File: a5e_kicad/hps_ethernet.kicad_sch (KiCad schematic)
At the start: 53 parts, among them J9 RJ45_RB1-125B8G1A, U10 RTL8211FDI-CG, Y3 25MHz

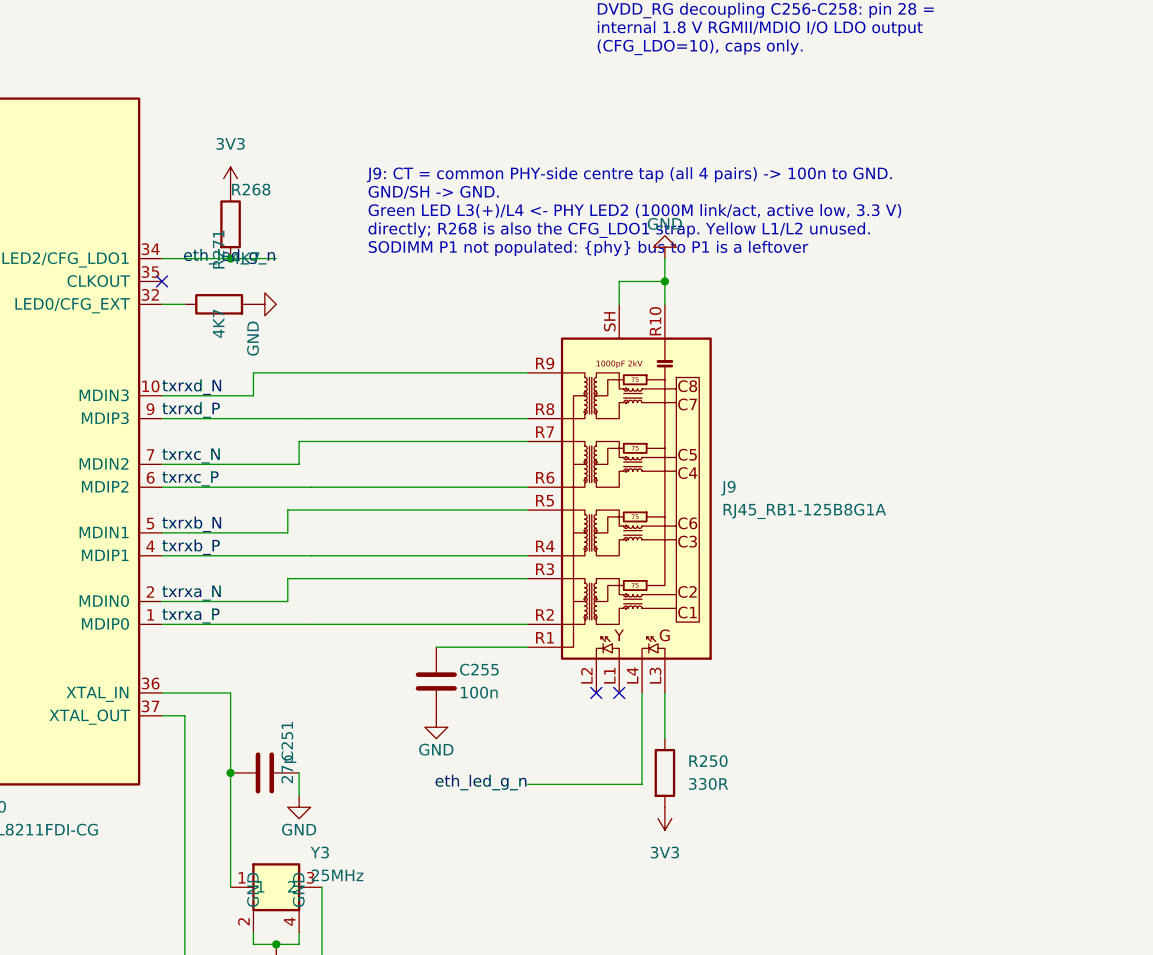
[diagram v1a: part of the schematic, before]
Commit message: J9 MagJack to HanRun HR911130A with the Zynq board's PHY layout
- J9: UDE RB1-125B8G1A (oversold at JLC) replaced by HanRun HR911130A
  (LCSC C54408), symbol and footprint from the Zynq board; nets eth_ct and
  eth_led_a named
- PHY area copied from the Zynq board: U10 rotated to 180 deg, passives in
  the Zynq positions, J9 at the Zynq edge offset, MDI pairs copied; block
  2 mm higher to clear U11. R251-R256 stay next to U10, C30-C32 under U10
- Old PHY-local routing, RGMII/MDIO pieces in the PHY area and conflicting
  GND/1V2 copper removed; RGMII/MDIO/PHY routing to redo
- Includes the pending board edits (zone refill etc.)

ERC 0, DRC parity 0. DRC (refilled) 150 vs 201 before; 44 new unconnected.
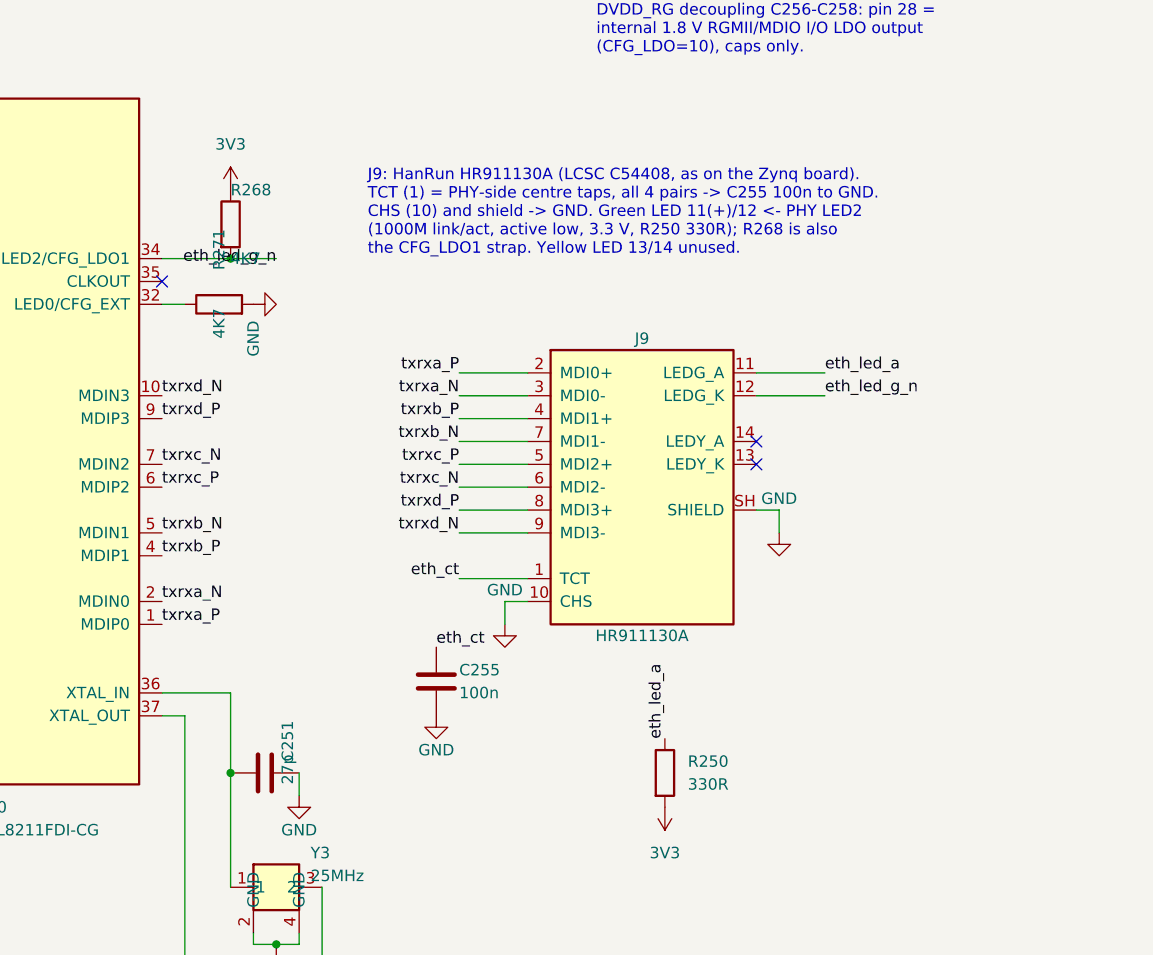
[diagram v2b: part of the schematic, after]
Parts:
- J9: value RJ45_RB1-125B8G1A -> HR911130A; footprint Connector_RJ:RJ45_UDE_RB1-125B8G1A -> agilex_lib:RJ45_Hanrun_HR911130A_Horizontal; symbol Connector:RJ45_RB1-125B8G1A -> agilex_5_lib:HR911130A; LCSC C363353 -> C54408
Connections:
- net GND: now also J9.10 (CHS); no longer J9.R10 (GND)
- net eth_led_g_n: now also J9.12 (LEDG_K); no longer J9.L4
- net txrxa_N: now also J9.3 (MDI0-); no longer J9.R3 (TD1-)
- net txrxa_P: now also J9.2 (MDI0+); no longer J9.R2 (TD1+)
- net txrxb_N: now also J9.7 (MDI1-); no longer J9.R5 (TD2-)
- net txrxb_P: now also J9.4 (MDI1+); no longer J9.R4 (TD2+)
- net txrxc_N: now also J9.6 (MDI2-); no longer J9.R7 (TD3-)
- net txrxc_P: now also J9.5 (MDI2+); no longer J9.R6 (TD3+)
- net txrxd_N: now also J9.9 (MDI3-); no longer J9.R9 (TD4-)
- net txrxd_P: now also J9.8 (MDI3+); no longer J9.R8 (TD4+)
- net eth_led_a: now reaches R250.1
- net eth_led_a: now also J9.11 (LEDG_A); no longer J9.L3
- net eth_ct: now reaches C255.1
- net eth_ct: now also J9.1 (TCT); no longer J9.R1 (CT)
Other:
- note added: "J9: HanRun HR911130A (LCSC C54408, as on the Zynq board). TCT (1) = PHY-side centre taps, all 4 pairs -> C255 100n to GND. CHS (10) and shield -> GND. Green LED 11(+)/12 <- PHY LED2 (1000M link/act, active low, 3.3 V, R250 330R); R268 is also the CFG_LDO1 strap. Yellow LED 13/14 unused."
- note removed: "J9: CT = common PHY-side centre tap (all 4 pairs) -> 100n to GND. GND/SH -> GND. Green LED L3(+)/L4 <- PHY LED2 (1000M link/act, active low, 3.3 V) directly; R268 is also the CFG_LDO1 strap. Yellow L1/L2 unused. SODIMM P1 not populated: {phy} bus to P1 is a leftover"

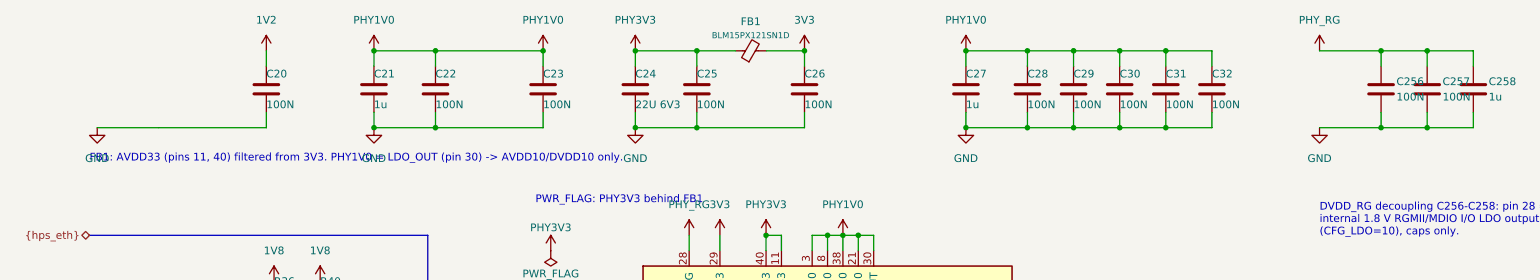
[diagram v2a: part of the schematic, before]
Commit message: Ethernet PHY: RGMII series resistors to 0201, decoupling one capacitor per pin
- R251-R262 (22R RGMII series) 0402 -> 0201, Yageo RC0201FR-0722RL (C155743); same positions, no copper attached
- removed C20 (100n on 1V2, no PHY pin uses it), C27 (second 1u on PHY1V0), C31/C32 (second caps on pins 8/38),
  C256 (second 100n on PHY_RG)
- C29 moved from PHY1V0 to PHY3V3: pin 40 (AVDD33) had no capacitor; on the board it already sits 1.4 mm from it
- per RTL8211F(D)(I)-CG data sheet Rev 1.7 9.2 and the Zynq board's U901 (ETH_PHY_REVIEW.md)
- ERC 0, schematic parity 0, DRC no new violations (unconnected 218 -> 208)
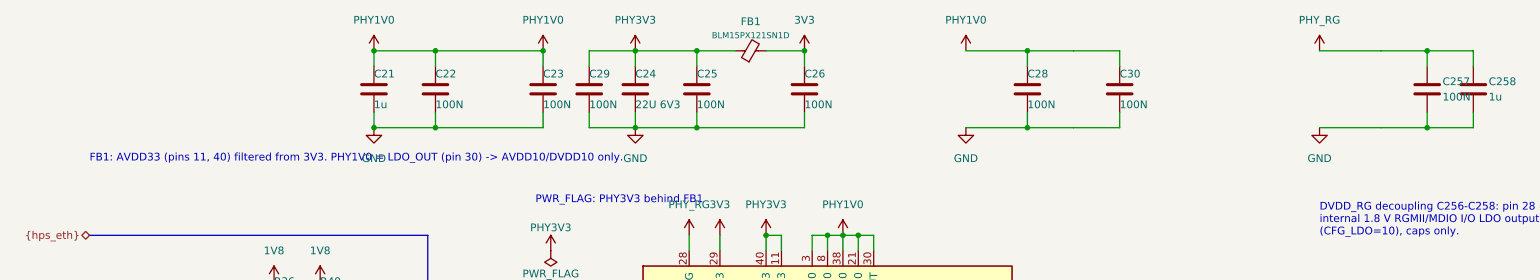
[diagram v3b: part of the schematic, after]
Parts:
- removed C20, C256, C31, C32: 100N, Capacitor_SMD:C_0402_1005Metric, symbol Device:C
- removed C27: 1u, Capacitor_SMD:C_0402_1005Metric, symbol Device:C
- R251, R252, R253, R254, R255, R256, R257, R258, R259, R260, R261, R262: footprint Resistor_SMD:R_0402_1005Metric -> Resistor_SMD:R_0201_0603Metric; LCSC C25092 -> C155743
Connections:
- net PHY1V0: no longer C29.1
- net PHY3V3: now also C29.1
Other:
- moved on the sheet: C29

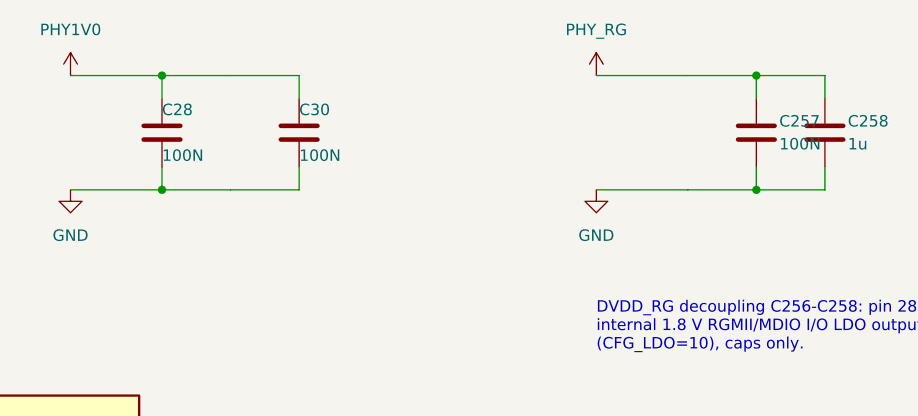
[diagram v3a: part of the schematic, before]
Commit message: Ethernet PHY passives to 0201, R27/R28 to 0402, preliminary RGMII routing
- 31 PHY passives on the hps_ethernet sheet 0402 -> 0201 (C24 22u stays
  0402): 100n C190183, 1u C272877, 27p C85899, 10k C473048,
  330R C516485, 4K7 C270346, 1K5 C270361, 2K49 C473476.
- Refclk bias R27/R28 0201 -> 0402 (C25120, 49.9R); R28 moved 0.1 mm
  to +x to clear the refclk_N meander.
- Preliminary RGMII routing: RX on F.Cu, TX on In2. Group spread
  TX 79 ps (TXD1 longest), RX 44 ps.
- Schematic sheets as saved by eeschema.
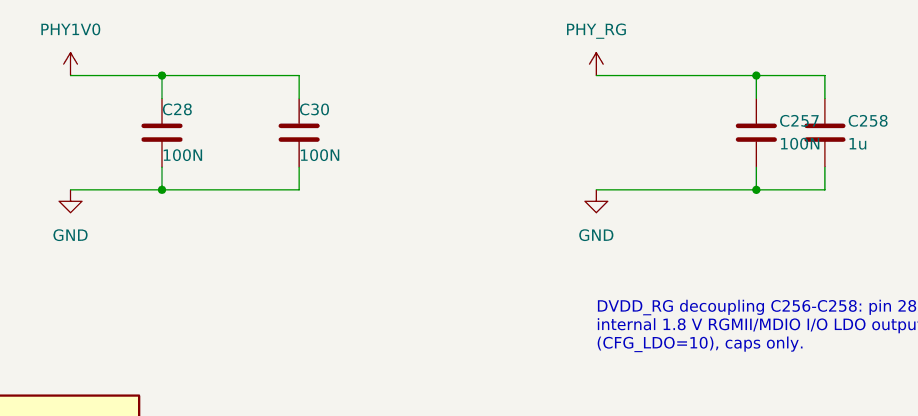
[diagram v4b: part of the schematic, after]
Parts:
- C21, C258, C259: footprint Capacitor_SMD:C_0402_1005Metric -> Capacitor_SMD:C_0201_0603Metric; LCSC C52923 -> C272877
- C22, C23, C25, C255, C257, C26, C28, C29, C30: footprint Capacitor_SMD:C_0402_1005Metric -> Capacitor_SMD:C_0201_0603Metric; LCSC C1525 -> C190183
- C251, C252: footprint Capacitor_SMD:C_0402_1005Metric -> Capacitor_SMD:C_0201_0603Metric; LCSC C1557 -> C85899
- R247: footprint Resistor_SMD:R_0402_1005Metric -> Resistor_SMD:R_0201_0603Metric; LCSC C25744 -> C473048
- R250: footprint Resistor_SMD:R_0402_1005Metric -> Resistor_SMD:R_0201_0603Metric; LCSC C25104 -> C516485
- R268, R269, R270, R271, R30, R31, R32, R33, R34, R35, R37, R39, R40: footprint Resistor_SMD:R_0402_1005Metric -> Resistor_SMD:R_0201_0603Metric; LCSC C25900 -> C270346
- R36: footprint Resistor_SMD:R_0402_1005Metric -> Resistor_SMD:R_0201_0603Metric; LCSC C25867 -> C270361
- R41: footprint Resistor_SMD:R_0402_1005Metric -> Resistor_SMD:R_0201_0603Metric; LCSC C25884 -> C473476
